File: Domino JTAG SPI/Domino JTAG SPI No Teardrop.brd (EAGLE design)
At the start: 25.4 x 33 mm, 26 parts, among them J1 MH10-1, J2 MH10-1, J3 MH2-1, J4 MH3-2, J5 MHRA7-2-0.1, SW1 IT-1124SMD

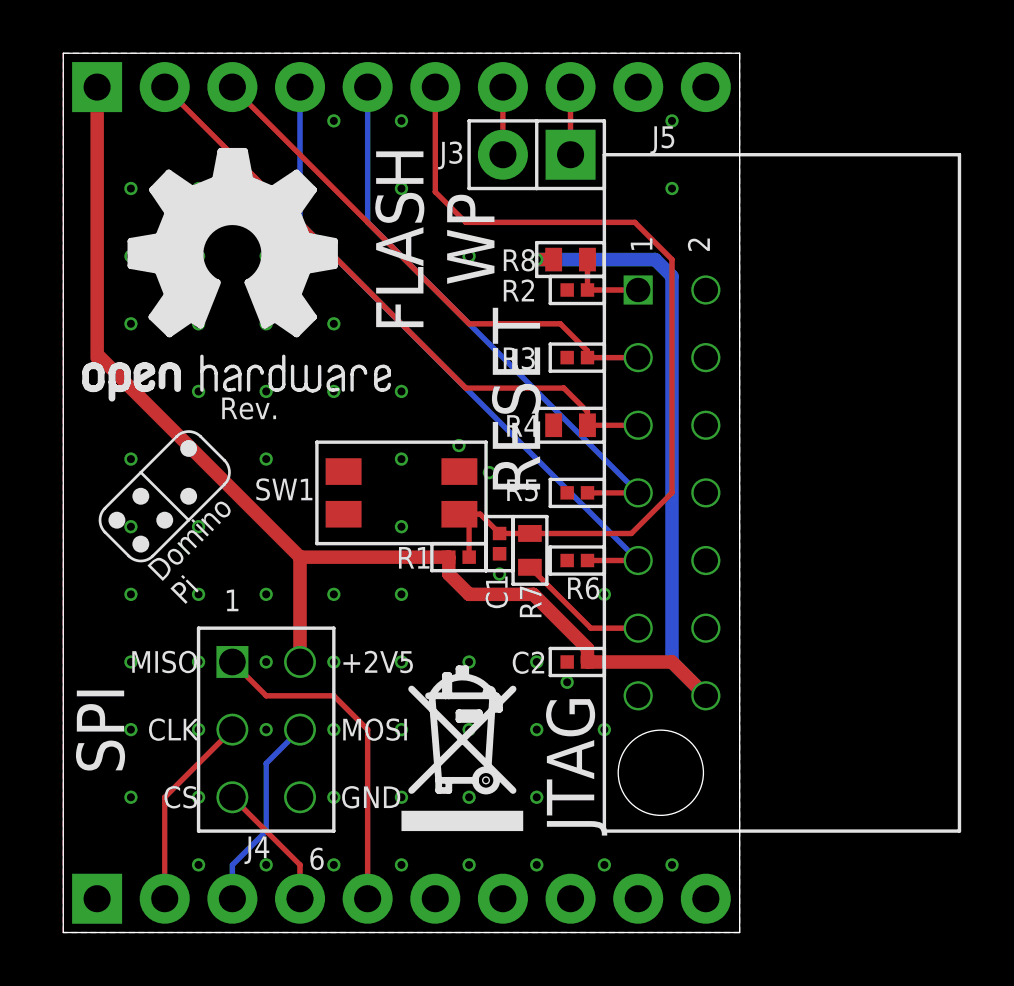
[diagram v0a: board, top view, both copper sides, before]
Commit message: Modified Domino Flash SPI tile to fit a standard SPI Flash jig and SPI Flash chip footprint
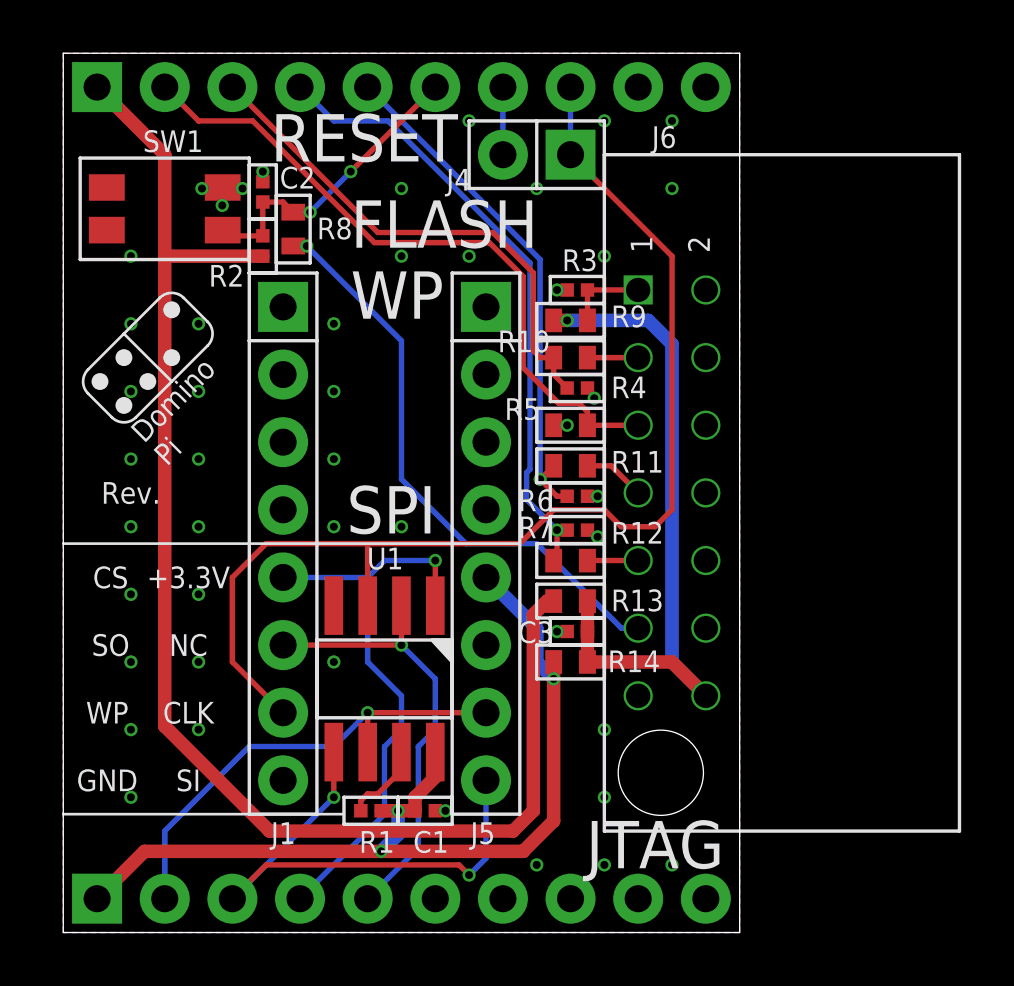
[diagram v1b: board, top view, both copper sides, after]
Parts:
- removed U$11: (no value), Domino:RECYCLE_BIN_LOGO
- removed U$12: (no value), Domino:OPEN_HARDWARE_LOGO
- added C3: 100n, Domino:C0402
- added J6: MHRA7-2-0.1, Domino:MHRA7-2-0.1
- added R10, R11, R12, R13, R14, R9: 0R, Domino:R0603
- added U1: SPI_FLASH, Domino:SOIC-8
- C1: value 10n -> 100n
- C2: value 100n -> 10n
- J1: value MH10-1 -> MH8-1; device Domino:MH10-1-0.1 -> Domino:MH8-1-0.1
- J3: value MH2-1 -> MH10-1; device Domino:MH2-1-0.1 -> Domino:MH10-1-0.1
- J4: value MH3-2 -> MH2-1; device Domino:MH3-2-0.1 -> Domino:MH2-1-0.1
- J5: value MHRA7-2-0.1 -> MH8-1; device Domino:MHRA7-2-0.1 -> Domino:MH8-1-0.1
- R4, R7: value 0R -> 10k; device Domino:R0603 -> Domino:R0402
- R5: value 10k -> 0R; device Domino:R0402 -> Domino:R0603
- moved J3 33.1 mm to (1.27, 1.27), flipped to the bottom
- moved J2 30.5 mm to (1.27, 31.8)
- moved J4 24.4 mm to (19.1, 29.2), turned to 180 degrees
- moved C2 21.2 mm to (7.49, 27.8), turned to 90 degrees
- moved U$4 17.3 mm to (12.2, 24.3)
- moved SW1 13.9 mm to (3.81, 27.2)
- moved U$8 13.6 mm to (6.73, 17.3)
- moved U$10 12.1 mm to (6.60, 22.5)
- moved R2 11.9 mm to (7.49, 25.8), turned to 270 degrees
- moved J1 10.8 mm to (8.26, 23.5), flipped to the top, turned to 270 degrees
- moved R8 10.5 mm to (8.64, 26.4), turned to 270 degrees
- moved C1 10.4 mm to (13.6, 4.57), turned to 180 degrees
- moved R1 10.1 mm to (11.6, 4.57)
- moved J5 9.88 mm to (15.9, 23.5)
- moved U$6 8.68 mm to (20.4, 9.53)
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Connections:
- new net +3V3: C1.2, J3.1, J5.5, R1.1, R14.2, U1.8
- new net N$2: J6.7, R11.2
- new net N$3: J6.9, R12.2
- new net N$4: R1.2, U1.7
- new net N$5: J6.3, R10.2
- new net VCC: C3.1, J6.14, R13.1, R14.1, R9.2
- net !JTAG_RESET: now also J6.11, R8.2; no longer J5.11, R7.2
- net !RESET_L: now also C2.1, J2.6, R2.1, R8.1; no longer C1.1, J1.6, R1.1, R7.1
- net +2V5: now also J2.1, R13.2, R2.2; no longer C2.1, J1.1, J4.2, J5.14, R1.2, R8.2
- net FLASH_WP: now also J1.7, J2.8, J4.1, U1.3; no longer J1.8, J3.1
- net GND: now also C1.1, C3.2, J1.8, J3.10, J3.6, J6.10, J6.2, J6.4, J6.6, J6.8, R7.1, U1.4; no longer C1.2, J1.10, J2.6, J4.6, J5.10, J5.2, J5.4, J5.6, J5.8, R2.1
- net GPIO24: now also J2.7, J4.2; no longer J1.7, J3.2
- net JTAG_TCK: now also J2.4, R12.1, R7.2; no longer J1.4, J5.9, R6.2
- net JTAG_TDI: now also J2.3, R10.1, R4.2; no longer J1.3, J5.3, R3.2
- net JTAG_TDO: now also J2.2, J6.5, R5.2; no longer J1.2, J5.5, R4.2
- net JTAG_TMS: now also J2.5, R11.1, R6.2; no longer J1.5, J5.7, R5.2
- net SPI_CLK: now also J3.2, J5.7, U1.6; no longer J2.2, J4.3
- net SPI_CS: now also J1.5, J3.4, U1.1; no longer J2.4, J4.5
- net SPI_MISO: now also J1.6, J3.5, U1.2; no longer J2.5, J4.1
- net SPI_MOSI: now also J3.3, J5.8, U1.5; no longer J2.3, J4.4
- net TRST_L: now also J6.1, R3.2, R9.1; no longer J5.1, R2.2, R8.1
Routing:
- net FLASH_WP: track 2.54 -> 44.0 mm
- net +3V3: track 0.00 -> 34.8 mm, vias 0 -> 3
- net VCC: track 0.00 -> 25.8 mm, vias 0 -> 1
- net !RESET_L: track 33.3 -> 11.5 mm, vias 0 -> 2
- net SPI_CS: track 4.86 -> 21.8 mm, vias 0 -> 1
- net !JTAG_RESET: track 5.01 -> 21.9 mm, vias 0 -> 1
- net SPI_MOSI: track 7.40 -> 20.5 mm, vias 0 -> 2
- net +2V5: track 65.1 -> 53.9 mm, vias 1 -> 0
- net SPI_CLK: track 7.40 -> 17.9 mm, vias 0 -> 1
- net SPI_MISO: track 12.5 -> 17.0 mm, vias 0 -> 1
- net N$4: track 0.00 -> 3.06 mm
- net N$2: track 0.00 -> 2.33 mm
- net JTAG_TDO: track 23.3 -> 25.3 mm
- net JTAG_TMS: track 21.4 -> 19.4 mm, vias 0 -> 1
- net N$5: track 0.00 -> 1.91 mm
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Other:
- board text added: "+3.3V"
- board text added: "+3V3"
- board text added: "NC"
- board text added: "SI"
- board text added: "SO"
- board text added: "WP"

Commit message: Added series resistors on SPI Flash SO in Domino JTAG SPI tile
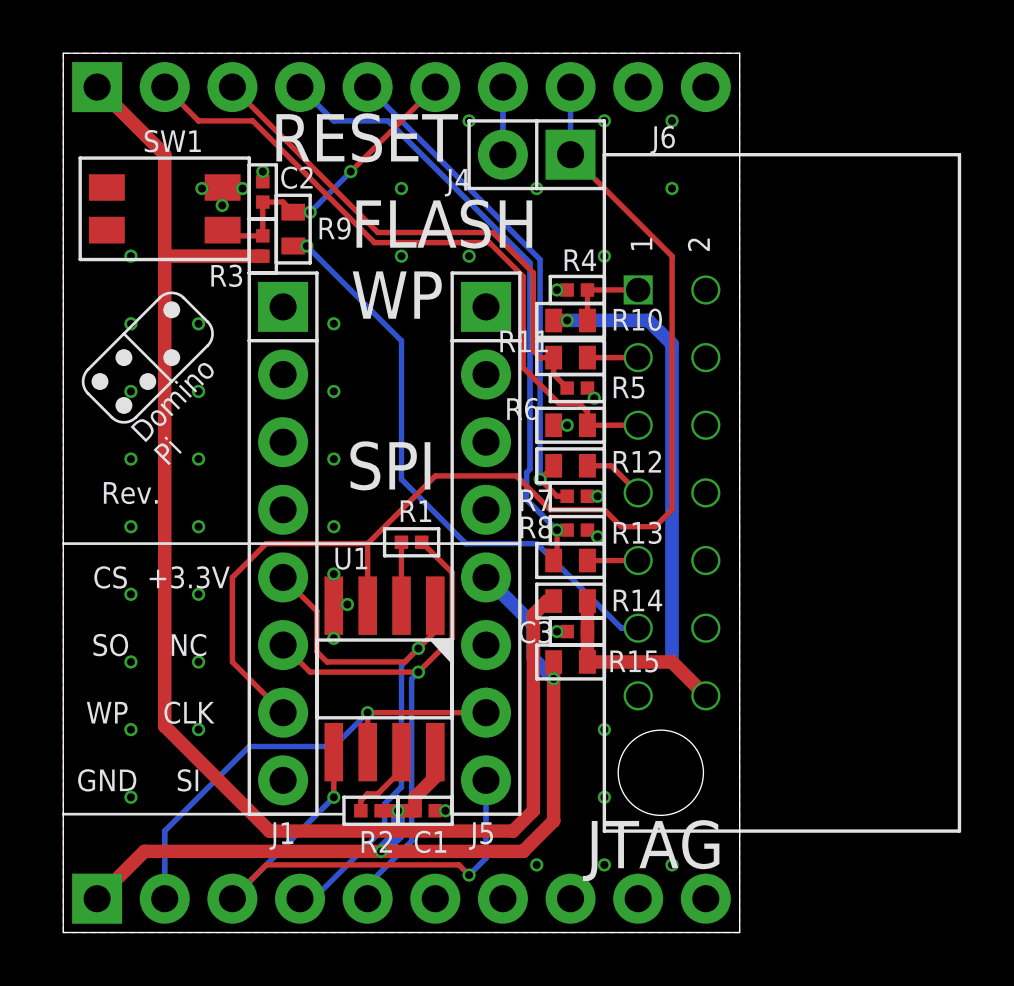
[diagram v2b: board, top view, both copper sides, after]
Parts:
- added R15: 0R, Domino:R0603
- R1: value 10k -> 1k
- R5, R8: value 0R -> 10k; device Domino:R0603 -> Domino:R0402
- R6: value 10k -> 0R; device Domino:R0402 -> Domino:R0603
- moved R2 21.6 mm to (11.6, 4.57), turned to 180 degrees
- moved R8 15.5 mm to (19.3, 15.1), turned to 180 degrees
- moved R3 11.9 mm to (7.49, 25.8), turned to 270 degrees
- moved R9 11.0 mm to (8.64, 26.4), turned to 270 degrees
- moved R1 10.2 mm to (13.1, 14.7), turned to 0 degrees
- moved R11 4.06 mm to (19.1, 21.6)
- moved R4 3.68 mm to (19.3, 24.1), turned to 0 degrees
- moved R12 3.56 mm to (19.1, 17.5)
- moved R6 2.68 mm to (19.1, 19.1), turned to 0 degrees
- moved R14 2.29 mm to (19.1, 12.4)
- moved R13 1.52 mm to (19.1, 14.0), turned to 0 degrees
- moved R5 1.42 mm to (19.3, 20.4), turned to 180 degrees
- moved R10 1.40 mm to (19.1, 23.0), turned to 180 degrees
- moved R7 1.27 mm to (19.3, 16.4)
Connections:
- new net N$6: R1.1, U1.2
- net !JTAG_RESET: now also R9.2; no longer R8.2
- net !RESET_L: now also R3.1, R9.1; no longer R2.1, R8.1
- net +2V5: now also R14.2, R3.2; no longer R13.2, R2.2
- net +3V3: now also R15.2, R2.1; no longer R1.1, R14.2
- net GND: now also R8.1; no longer R3.1
- net JTAG_TCK: now also R13.1, R8.2; no longer R12.1, R7.2
- net JTAG_TDI: now also R11.1, R5.2; no longer R10.1, R4.2
- net JTAG_TDO: now also R6.2; no longer R5.2
- net JTAG_TMS: now also R12.1, R7.2; no longer R11.1, R6.2
- net N$2: now also R12.2; no longer R11.2
- net N$3: now also R13.2; no longer R12.2
- net N$4: now also R2.2; no longer R1.2
- net N$5: now also R11.2; no longer R10.2
- net SPI_MISO: now also R1.2; no longer U1.2
- net TRST_L: now also R10.1, R4.2; no longer R3.2, R9.1
- net VCC: now also R10.2, R15.1; no longer R13.1, R9.2
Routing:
- net SPI_MISO: track 17.0 -> 20.7 mm
- net N$6: track 0.00 -> 2.38 mm
- net FLASH_WP: track 44.0 -> 45.0 mm
- net SPI_CS: track 21.8 -> 20.9 mm
